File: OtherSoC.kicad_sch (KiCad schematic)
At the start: 1 part, among them U2 rv1126/rv1109

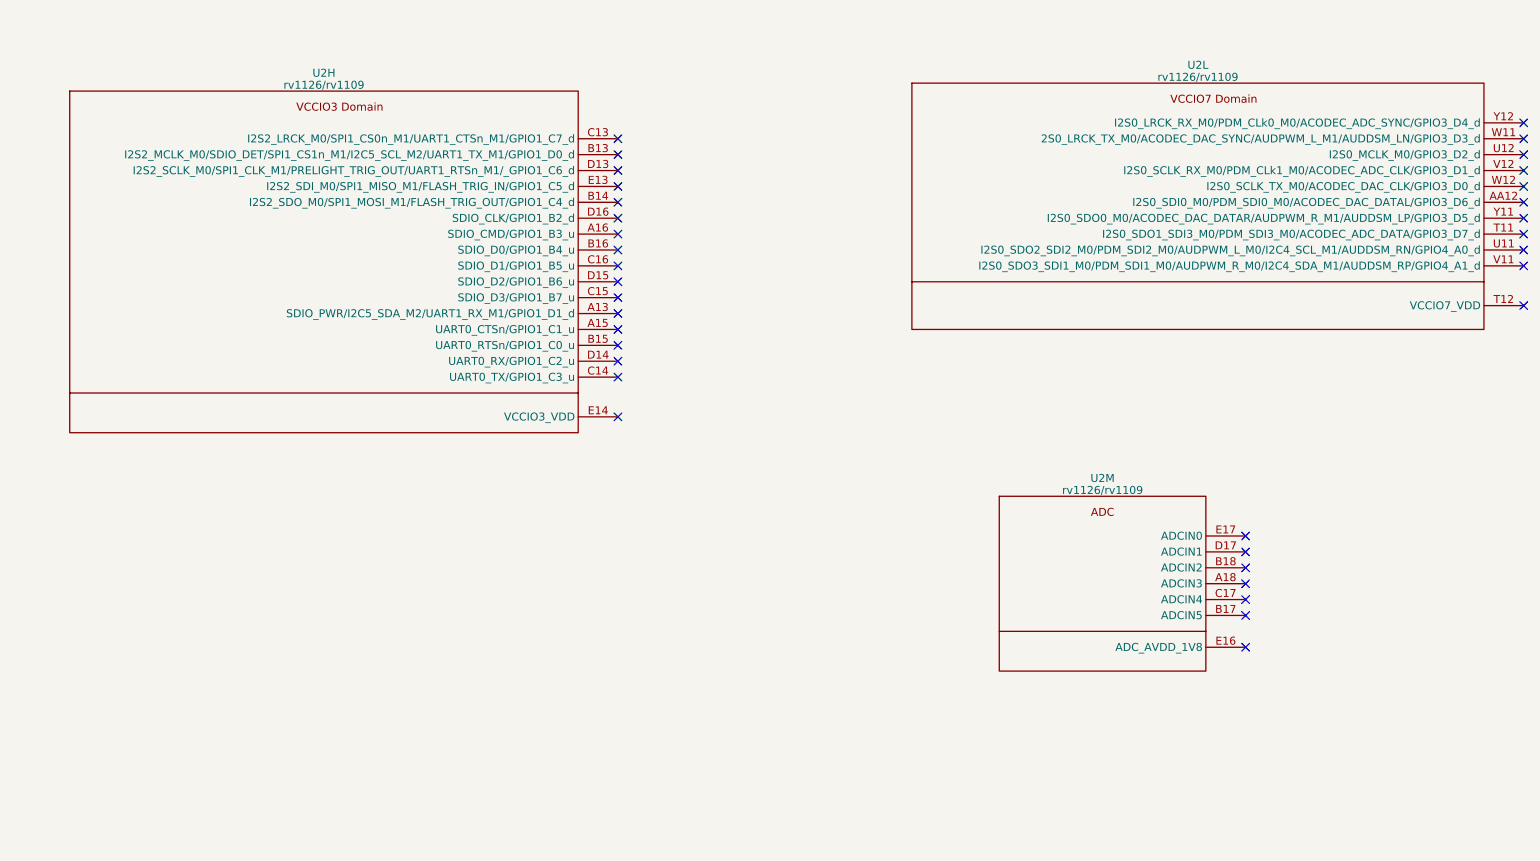
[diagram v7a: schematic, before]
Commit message: replaced Leaf specified symbols with unified iotpi symbols
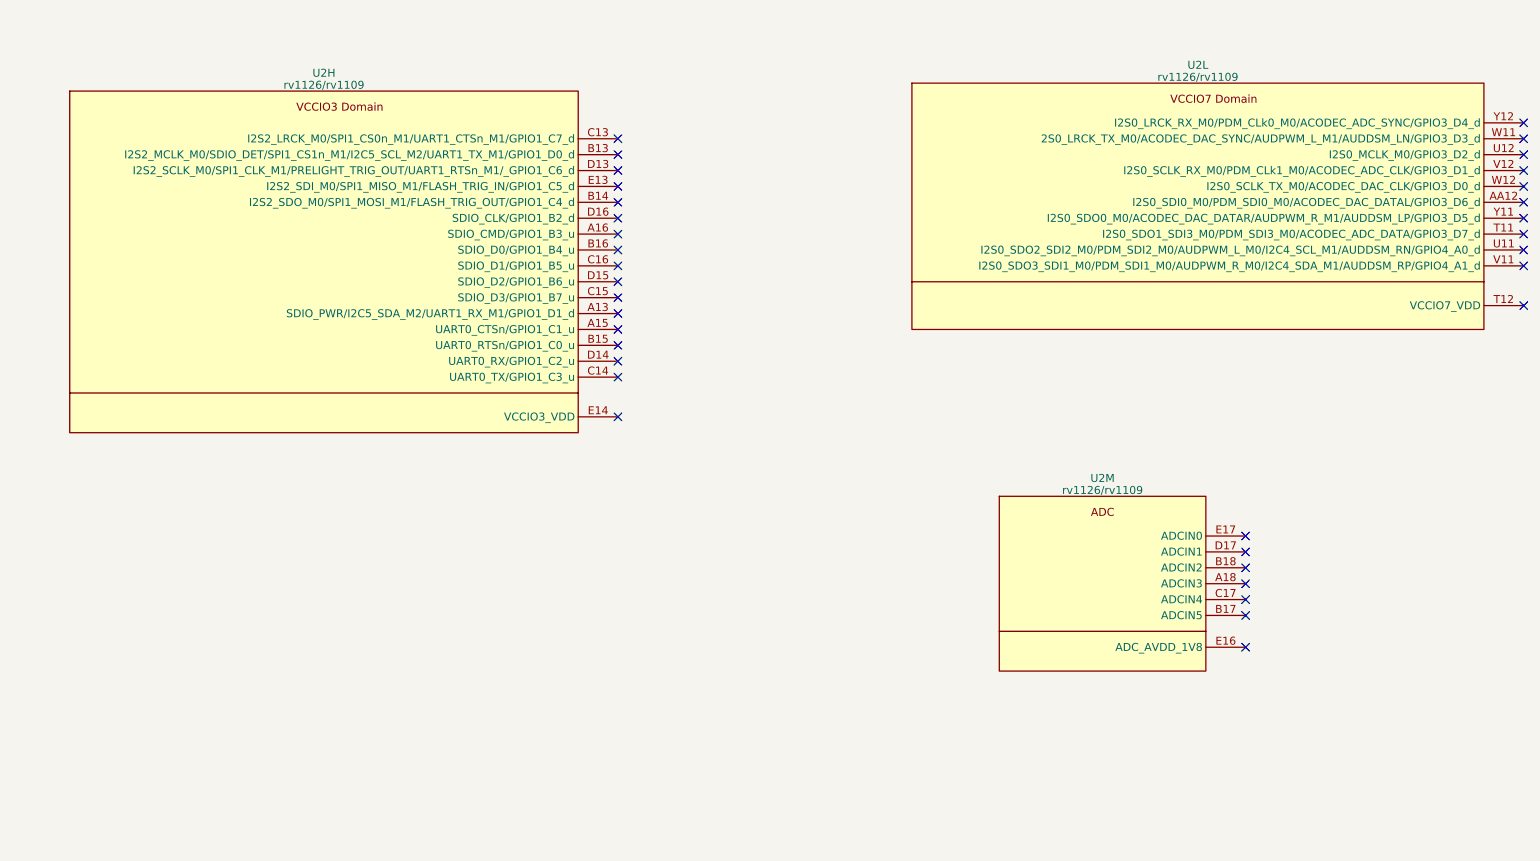
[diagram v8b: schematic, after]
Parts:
- U2: symbol CPU_Rockchip:rv1126_rv1109 -> IotPi_CPU_Rockchip:rv1126_rv1109
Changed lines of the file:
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@@
   (no_connect (at 114.3 48.26))
   (no_connect (at 259.08 58.42))
-  (symbol (lib_id "CPU_Rockchip:rv1126_rv1109") (at 191.77 106.68 0) (unit 13)
+  (symbol (lib_id "IotPi_CPU_Rockchip:rv1126_rv1109") (at 191.77 106.68 0) (unit 13)
     (in_bom yes) (on_board yes) (dnp no) (fields_autoplaced)
     (property "Reference" "U2" (at 191.77 92.3671 0)
@@
       (effects (font (size 1.27 1.27)))
     )
-    (property "Footprint" "Rockchip_SoC:Rockchip_RV1126_FCCSP409LD_14.0x14.0mm" (at 223.52 133.35 0)
-      (effects (font (size 1.27 1.27)) hide)
-    )
-    (property "Datasheet" "" (at 223.52 133.35 0)
+    (property "Footprint" "Rockchip_SoC:Rockchip_RV1126_FCCSP409LD_14.0x14.0mm" (at 223.52 153.67 0)
+      (effects (font (size 1.27 1.27)) hide)
+    )
+    (property "Datasheet" "" (at 223.52 153.67 0)
       (effects (font (size 1.27 1.27)) hide)
     )
@@
     )
   )
-  (symbol (lib_id "CPU_Rockchip:rv1126_rv1109") (at 67.31 46.99 0) (unit 8)
+  (symbol (lib_id "IotPi_CPU_Rockchip:rv1126_rv1109") (at 67.31 46.99 0) (unit 8)
     (in_bom yes) (on_board yes) (dnp no) (fields_autoplaced)
     (property "Reference" "U2" (at 67.31 27.5971 0)
@@
       (effects (font (size 1.27 1.27)))
     )
-    (property "Footprint" "Rockchip_SoC:Rockchip_RV1126_FCCSP409LD_14.0x14.0mm" (at 99.06 73.66 0)
-      (effects (font (size 1.27 1.27)) hide)
-    )
-    (property "Datasheet" "" (at 99.06 73.66 0)
+    (property "Footprint" "Rockchip_SoC:Rockchip_RV1126_FCCSP409LD_14.0x14.0mm" (at 99.06 93.98 0)
+      (effects (font (size 1.27 1.27)) hide)
+    )
+    (property "Datasheet" "" (at 99.06 93.98 0)
       (effects (font (size 1.27 1.27)) hide)
     )
@@
     )
   )
-  (symbol (lib_id "CPU_Rockchip:rv1126_rv1109") (at 207.01 49.53 0) (unit 12)
+  (symbol (lib_id "IotPi_CPU_Rockchip:rv1126_rv1109") (at 207.01 49.53 0) (unit 12)
     (in_bom yes) (on_board yes) (dnp no) (fields_autoplaced)
     (property "Reference" "U2" (at 207.01 26.3271 0)
@@
       (effects (font (size 1.27 1.27)))
     )
-    (property "Footprint" "Rockchip_SoC:Rockchip_RV1126_FCCSP409LD_14.0x14.0mm" (at 238.76 76.2 0)
-      (effects (font (size 1.27 1.27)) hide)
-    )
-    (property "Datasheet" "" (at 238.76 76.2 0)
-      (effects (font (size 1.27 1.27)) hide)
-    )
+    (property "Footprint" "Rockchip_SoC:Rockchip_RV1126_FCCSP409LD_14.0x14.0mm" (at 238.76 96.52 0)
+      (effects (font (size 1.27 1.27)) hide)
+    )
+    (property "Datasheet" "" (at 238.76 96.52 0)
+      (effects (font (size 1.27 1.27)) hide)
+    )
